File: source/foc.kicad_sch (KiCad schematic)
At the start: 26 parts, among them J1 Conn_01x03, J2 Conn_01x06, J3 Conn_01x08, J4 NRF wireless, P1 SWD, SW1 SW_DPDT_x2, U1 BMI160

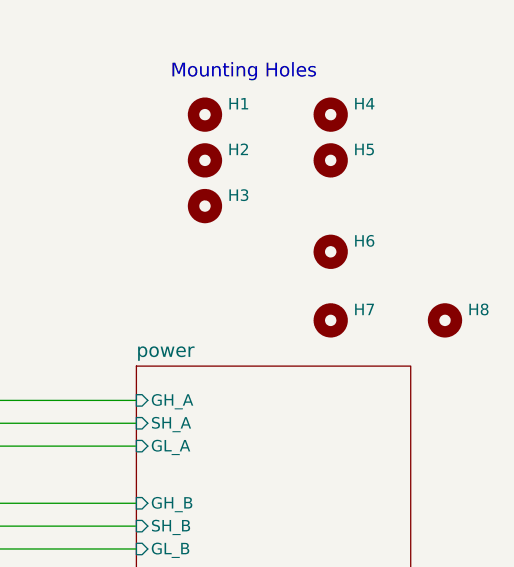
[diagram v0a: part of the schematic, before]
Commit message: 4 layer design
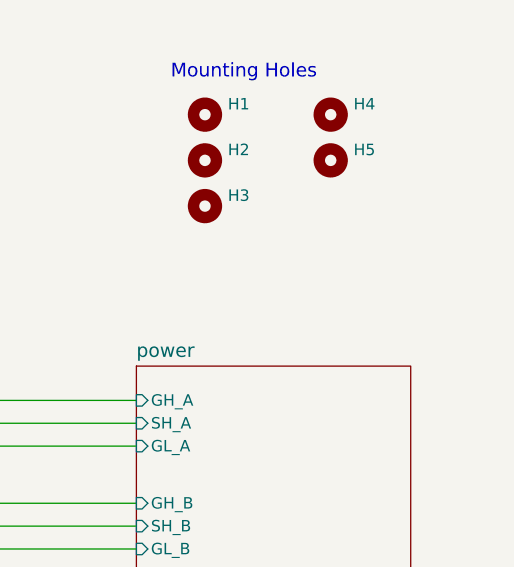
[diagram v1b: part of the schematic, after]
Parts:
- removed H6, H7, H8: MountingHole, MountingHole:MountingHole_4.3mm_M4_Pad_TopOnly, symbol Mechanical:MountingHole

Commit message: First 4 layer order at JLCPCB
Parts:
- removed J4: NRF wireless, Connector_PinSocket_2.54mm:PinSocket_2x04_P2.54mm_Vertical, symbol Connector_Generic:Conn_02x04_Odd_Even
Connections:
- no-connect marks 17 -> 16
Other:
- sheet mcu ports: added none; removed NRF_CSN, NRF_MISO, NRF_MOSI, NRF_SCK

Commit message: Add files via upload
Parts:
- removed H3: MountingHole, MountingHole:MountingHole_3.2mm_M3, symbol Mechanical:MountingHole
- renumbered H4 to H3, H5 to H4

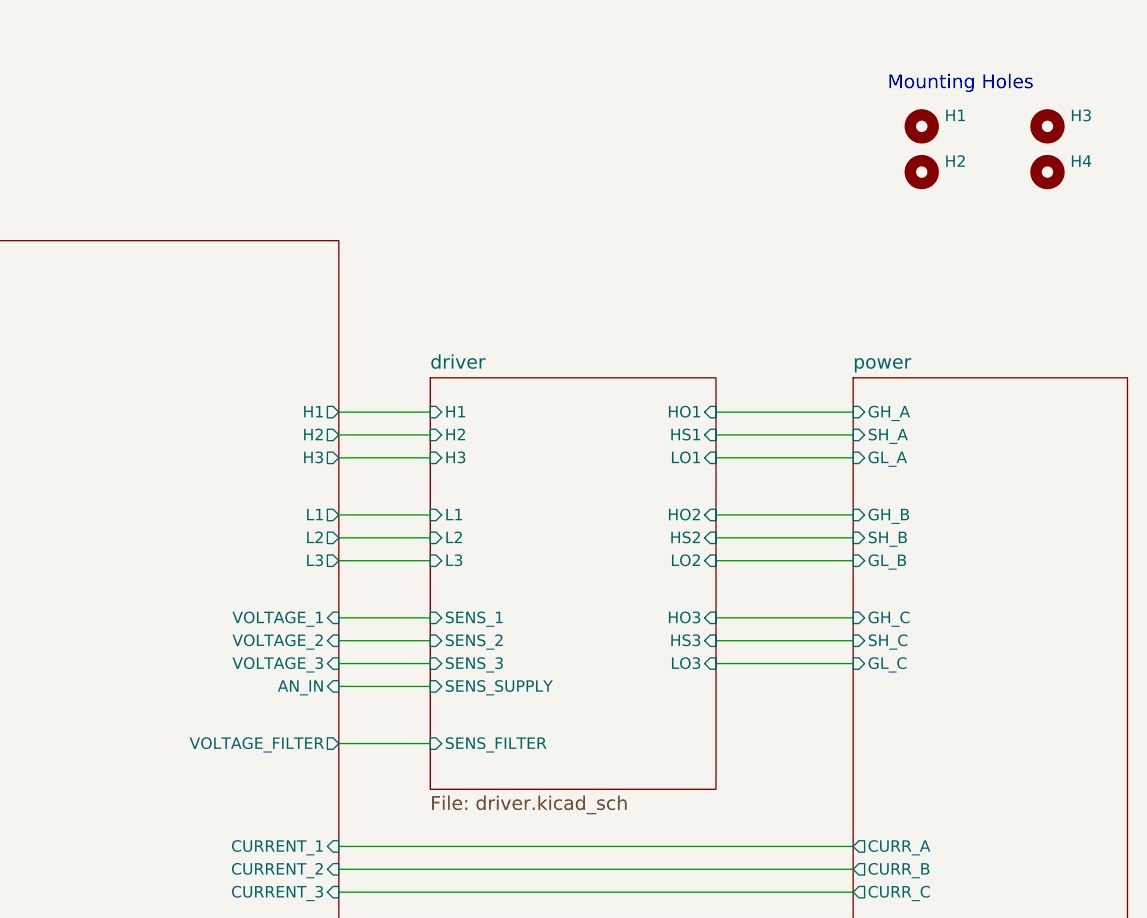
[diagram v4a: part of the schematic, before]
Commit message: Add files via upload
Filter resistor on current op-amps changed from 30k to 150R
Mosfets at 45 deg angle
Changed layout of power supply
Cut through center of board
Unnecessary components near mosfets removed
Voltage filters removed again
Crystal suspected noise source - moved to back of board
Current sensing moved to in0 - in2 (PA0-PA2)
Voltage sensing moved to in11-in13
Supply voltage moved to in10
Mosfets can now be attached to heat-sink plate using screws (that can be tightened throug holes in the board)
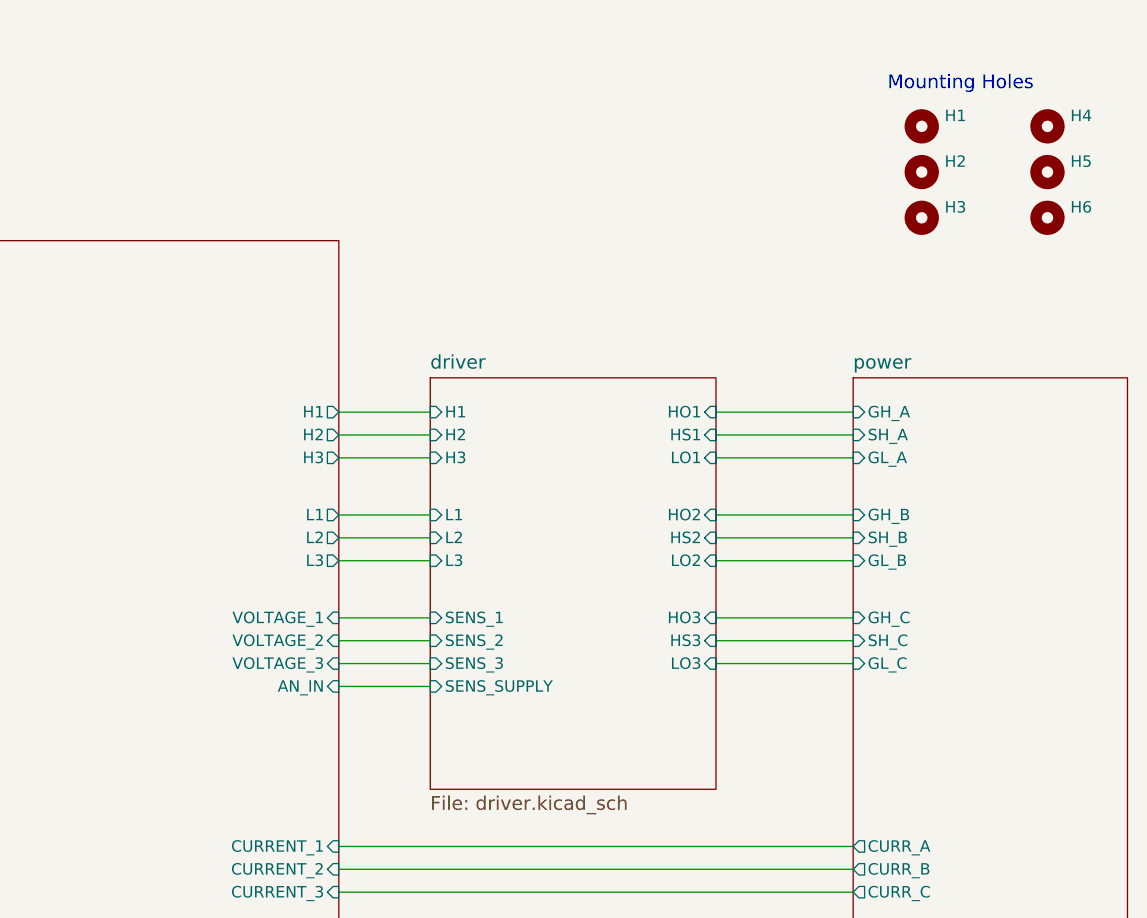
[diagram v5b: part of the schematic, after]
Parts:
- added H3, H6: MountingHole, MountingHole:MountingHole_3.2mm_M3, symbol Mechanical:MountingHole
- renumbered H3 to H4, H4 to H5
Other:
- sheet driver ports: added none; removed SENS_FILTER
- sheet mcu ports: added none; removed VOLTAGE_FILTER

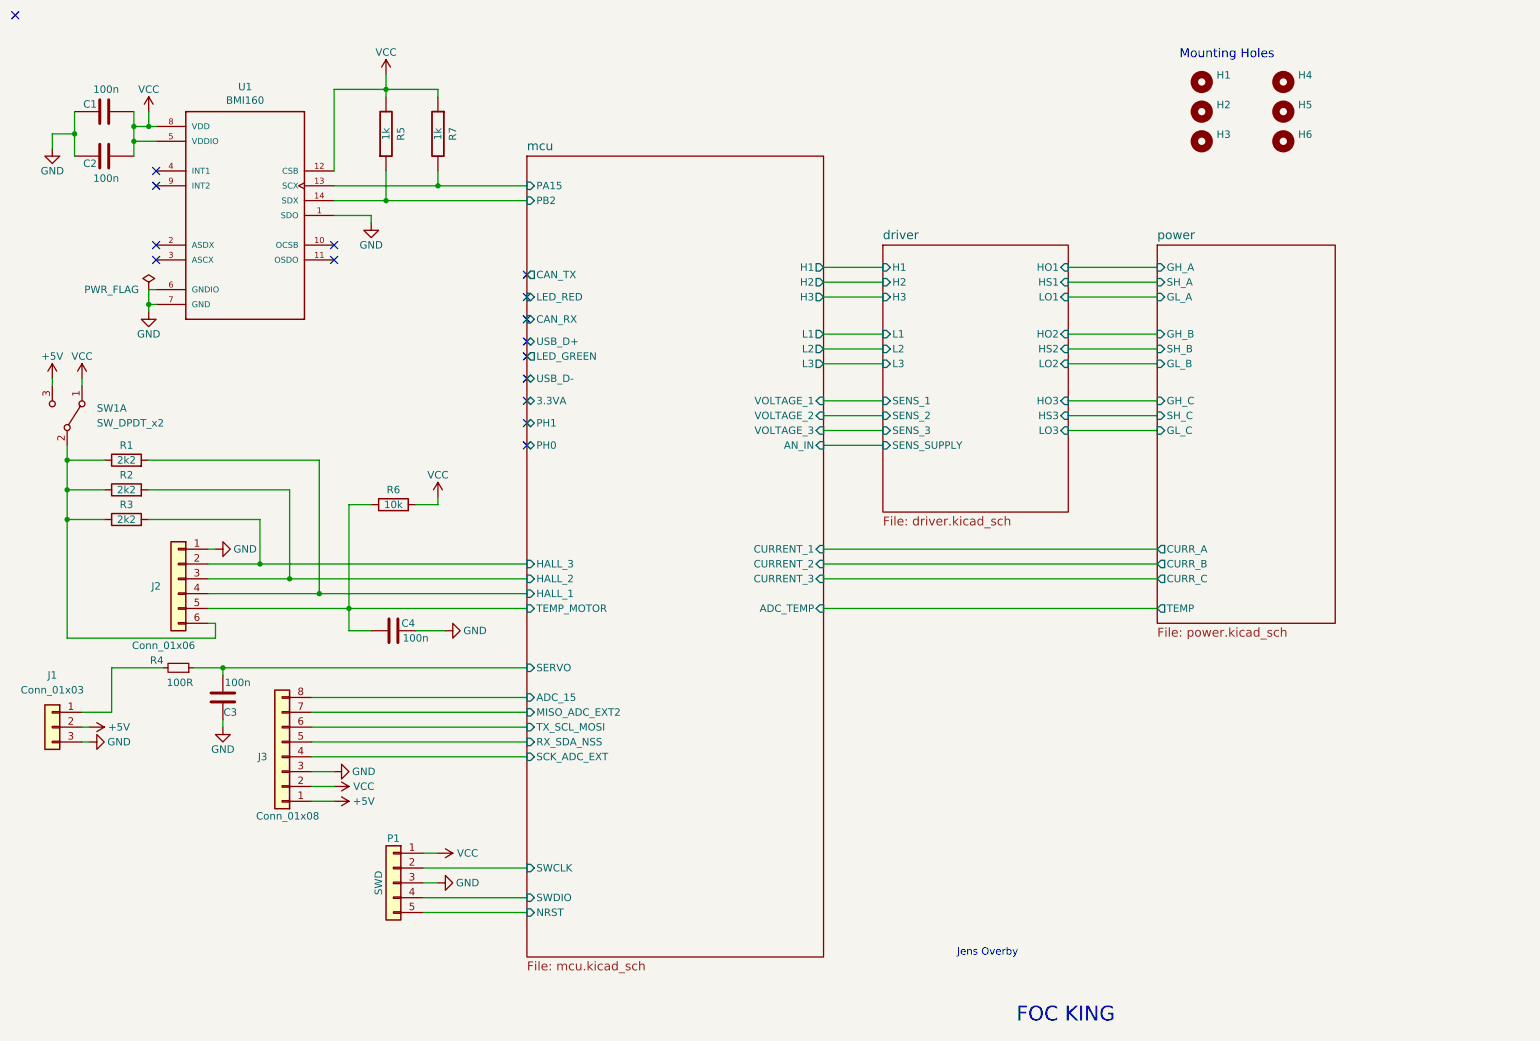
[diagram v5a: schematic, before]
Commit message: 2 board setup with mcu and foc shield separated
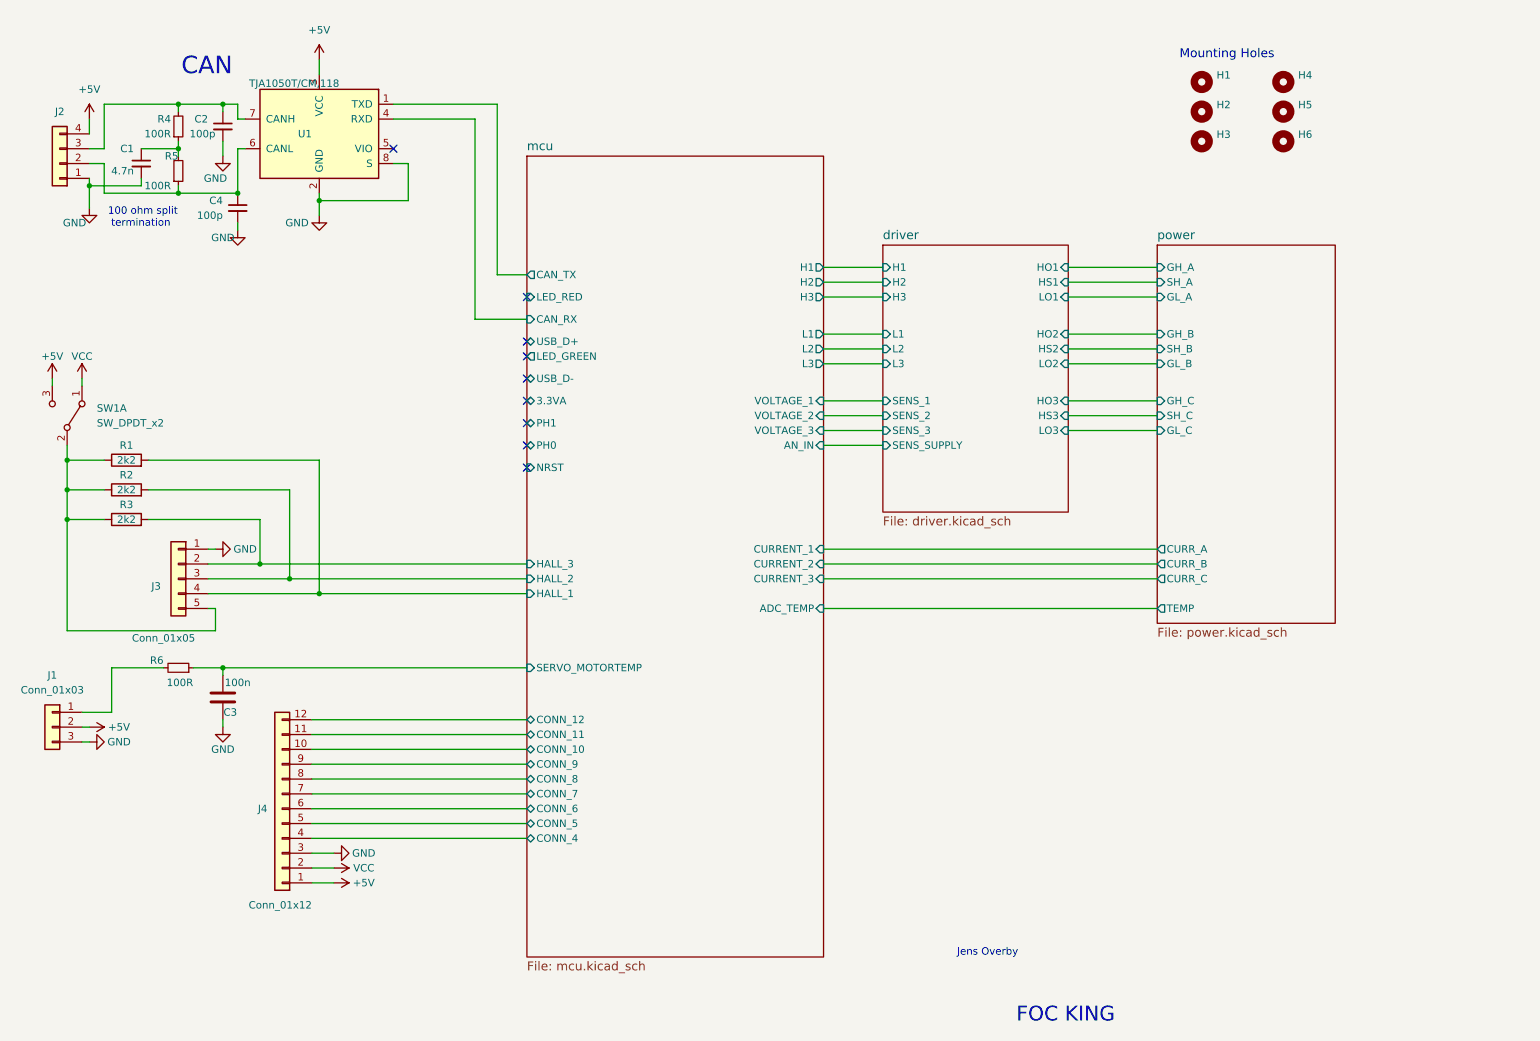
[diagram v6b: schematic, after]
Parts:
- removed C1, C2: 100n, Capacitor_SMD:C_0603_1608Metric, symbol BLDC_4-rescue:C-RESCUE-BLDC_4
- removed C4: 100n, Resistor_SMD:R_0603_1608Metric, symbol Device:C
- removed P1: SWD, Connector_PinHeader_2.54mm:PinHeader_1x05_P2.54mm_Vertical, symbol Connector_Generic:Conn_01x05
- removed R5, R7: 1k, Resistor_SMD:R_0603_1608Metric, symbol BLDC_4-rescue:R-RESCUE-BLDC_4
- removed R6: 10k, Resistor_SMD:R_0603_1608Metric, symbol Device:R
- removed U1: BMI160, Package_LGA:Bosch_LGA-14_3x2.5mm_P0.5mm, symbol Cheap-FOCer-2-60mm-rescue:BMI160-IMU
- added C1: 4.7n, Capacitor_SMD:C_0603_1608Metric, symbol Device:C_Small
- added C2, C4: 100p, Capacitor_SMD:C_0603_1608Metric, symbol Device:C_Small
- added J2: Conn_01x04_Male, Connector_JST:JST_PH_B4B-PH-K_1x04_P2.00mm_Vertical, symbol Connector_Generic:Conn_01x04
- added R4, R5: 100R, Resistor_SMD:R_0603_1608Metric, symbol Device:R_Small
- added U1: TJA1050T/CM,118, Package_SO:SOIC-8_3.9x4.9mm_P1.27mm, symbol Interface_CAN_LIN:TJA1051T-3
- J3: renamed from J2; value Conn_01x06 -> Conn_01x05; footprint Connector_JST:JST_PH_B6B-PH-K_1x06_P2.00mm_Vertical -> Connector_JST:JST_PH_B5B-PH-K_1x05_P2.00mm_Vertical; symbol Connector_Generic:Conn_01x06 -> Connector_Generic:Conn_01x05
- J4: renamed from J3; value Conn_01x08 -> Conn_01x12; footprint Connector_JST:JST_PH_B8B-PH-K_1x08_P2.00mm_Vertical -> Connector_JST:JST_PH_B12B-PH-K_1x12_P2.00mm_Vertical; symbol Connector_Generic:Conn_01x08 -> Connector_Generic:Conn_01x12
- renumbered R4 to R6
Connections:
- net mcu/TEMP_MOTOR is gone; now on an unnamed net: J3.5 (Pin_5)
- net +5V: now also J2.4 (Pin_4), U1.3 (VCC)
- net GND: now also C1.2, C2.2, C4.2, J2.1 (Pin_1), U1.2 (GND), U1.8 (S)
- net mcu/CAN_RX: now also U1.4 (RXD)
- net mcu/CAN_TX: now also U1.1 (TXD)
- net at R1.1, R2.1, R3.1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: no longer J3.6 (Pin_6)
- net mcu/ADC_15 renamed mcu/CONN_8
- net mcu/MISO_ADC_EXT2 renamed mcu/CONN_7
- net mcu/RX_SDA_NSS renamed mcu/CONN_5
- net mcu/SCK_ADC_EXT renamed mcu/CONN_4
- net mcu/SERVO renamed mcu/SERVO_MOTORTEMP
- net mcu/TX_SCL_MOSI renamed mcu/CONN_6
- new net: C2.1, J2.3 (Pin_3), R4.2, U1.7 (CANH)
- new net: C4.1, J2.2 (Pin_2), R5.1, U1.6 (CANL)
- new net: C1.1, R4.1, R5.2
- new net mcu/CONN_10: J4.10 (Pin_10)
- new net mcu/CONN_11: J4.11 (Pin_11)
- new net mcu/CONN_12: J4.12 (Pin_12)
- new net mcu/CONN_9: J4.9 (Pin_9)
- no-connect marks 16 -> 9
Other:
- sheet mcu ports: added CONN_10, CONN_11, CONN_12, CONN_4, CONN_5, CONN_6, CONN_7, CONN_8, CONN_9, SERVO_MOTORTEMP; removed ADC_15, MISO_ADC_EXT2, PA15, PB2, RX_SDA_NSS, SCK_ADC_EXT, SERVO, SWCLK, SWDIO, TEMP_MOTOR, TX_SCL_MOSI
- note added: "100 ohm split termination"
- note added: "CAN"
